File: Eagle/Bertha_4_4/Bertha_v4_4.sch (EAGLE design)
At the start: 115 parts, among them CON1 JACK_DC_BARREL, IC1 MCP1703DB, J1 RJ12RIGHTANGLE-I2C, J2 RJ12RIGHTANGLE-I2C, J7 22--02, Q1 BSP75, Q2 BSP75, Q3 BSP75, Q4 BSP75, Q5 BSP75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

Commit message: Added protection diode on 12V line closes #26
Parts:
- added D1: 1N581D1206, lpatiny:1N581D1206
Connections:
- new net VDD: C1.1, CU3.1, CU7.1, D1.C, D2.C, D4.C, IC1.VI, R12.2, X3-1.1, X3-2.1
- net +12V: now also D1.A; no longer C1.1, CU3.1, CU7.1, D2.C, D4.C, IC1.VI, R12.2, X3-1.1, X3-2.1
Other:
- moved on the sheet: C1, C2, CU3, CU4

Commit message: Added jack connector for PID closes #40
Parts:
- removed J7: 22--02, lpatiny:22--02
- added CON2: JACK_DC_BARREL, lpatiny:JACK_DC_BARREL
- C1, C10, C11, C12, C13, C2, C3, C4, C5, C6, C7, C8, C9, CU1, CU2, CU3, CU4, CU9, CX1, CX2: device rcl:C-EUC1206 -> rcl:C-EUC0805
- RT1, RT2: device resistor:R-EU_R1206 -> resistor:R-EU_R0805
- RUSB1, RUSB2: device resistor:R-EU_M1206 -> resistor:R-EU_M0805
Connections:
- removed net N$36: HX1.D, J7-2.S
- new net N$2: CON2.V+, HX1.D
- net +12V: now also CON2.GND; no longer J7-1.S

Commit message: Changed pin Mapping to allow PWM food control Need to Adapat Arduino code !!!
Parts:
- removed LORA_RST: (no value), Headerlibrary:PINHD-1X1
- CU7, CU8: device rcl:C-EUC1206 -> rcl:C-EUC0805
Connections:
- removed net N$10: R3.1, U$1.CS
- new net MEM_SEL: LDMEM.C, R3.1, U$1.CS
- net A2: now also 100K.2, U100.P$32; no longer R5.1
- net A3: now also R3.2; no longer R6.1
- net D10*: now also R5.1; no longer LDMEM.C, R3.2
- net D5*: now also R6.1; no longer 100K.2, LORA_RST.1, U100.P$32
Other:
- note removed: "LEVEL_Converters"
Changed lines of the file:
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@@
 <part name="GND7" library="supply1" deviceset="GND" device=""/>
 <part name="R1" library="rcl" deviceset="R-EU_" device="R0805" value="1k"/>
-<part name="CU7" library="rcl" deviceset="C-EU" device="C1206" value="10uF"/>
+<part name="CU7" library="rcl" deviceset="C-EU" device="C0805" value="10uF"/>
 <part name="GND19" library="supply1" deviceset="GND" device=""/>
-<part name="CU8" library="rcl" deviceset="C-EU" device="C1206" value="10uF"/>
+<part name="CU8" library="rcl" deviceset="C-EU" device="C0805" value="10uF"/>
 <part name="IC1" library="linear" deviceset="MCP1703" device="DB"/>
 <part name="P+15" library="SparkFun" deviceset="3.3V" device=""/>
@@
 <part name="SJ3" library="jumper" deviceset="SJ" device=""/>
 <part name="U100" library="Octanis1" deviceset="RN2483" device="" value="RN2483"/>
-<part name="LORA_RST" library="Headerlibrary" deviceset="PINHD-1X1" device=""/>
 <part name="GND32" library="supply1" deviceset="GND" device=""/>
 <part name="GND38" library="supply1" deviceset="GND" device=""/>
@@
 <wire x1="48.26" y1="7.62" x2="48.26" y2="68.58" width="1.27" layer="94"/>
 <wire x1="180.34" y1="289.56" x2="299.72" y2="289.56" width="1.27" layer="94"/>
-<text x="106.68" y="60.96" size="5.08" layer="91">LEVEL_Converters</text>
 <wire x1="104.14" y1="68.58" x2="104.14" y2="7.62" width="1.27" layer="94"/>
 <text x="50.8" y="60.96" size="5.08" layer="91">FOOD</text>
@@
 <instance part="SJ3" gate="1" x="142.24" y="149.86" rot="R270"/>
 <instance part="U100" gate="G$1" x="210.82" y="256.54" rot="R270"/>
-<instance part="LORA_RST" gate="G$1" x="251.46" y="281.94"/>
 <instance part="GND32" gate="1" x="246.38" y="157.48" rot="R270"/>
 <instance part="GND38" gate="1" x="228.6" y="142.24"/>
@@
 </segment>
 <segment>
-<label x="114.3" y="20.32" size="1.778" layer="95"/>
-<label x="162.56" y="20.32" size="1.778" layer="95"/>
-<wire x1="114.3" y1="20.32" x2="170.18" y2="20.32" width="0.1524" layer="91"/>
-</segment>
-<segment>
 <pinref part="RK3" gate="G$1" pin="1"/>
 <wire x1="467.36" y1="246.38" x2="472.44" y2="246.38" width="0.1524" layer="91"/>
@@
 </segment>
 <segment>
-<label x="114.3" y="22.86" size="1.778" layer="95"/>
-<label x="162.56" y="22.86" size="1.778" layer="95"/>
-<wire x1="114.3" y1="22.86" x2="170.18" y2="22.86" width="0.1524" layer="91"/>
-</segment>
-<segment>
 <pinref part="U$1" gate="G$1" pin="MISO"/>
 <wire x1="421.64" y1="248.92" x2="396.24" y2="248.92" width="0.1524" layer="91"/>
@@
 </segment>
 <segment>
-<label x="114.3" y="25.4" size="1.778" layer="95"/>
-<label x="162.56" y="25.4" size="1.778" layer="95"/>
-<wire x1="114.3" y1="25.4" x2="170.18" y2="25.4" width="0.1524" layer="91"/>
-</segment>
-<segment>
 <label x="490.22" y="243.84" size="1.778" layer="95"/>
 <label x="459.74" y="243.84" size="1.778" layer="95"/>
@@
 </segment>
 <segment>
-<pinref part="R5" gate="G$1" pin="1"/>
-<wire x1="55.88" y1="50.8" x2="50.8" y2="50.8" width="0.1524" layer="91"/>
-<label x="50.8" y="50.8" size="1.778" layer="95"/>
+<pinref part="100K" gate="G$1" pin="2"/>
+<pinref part="U100" gate="G$1" pin="P$32"/>
+<wire x1="226.06" y1="284.48" x2="226.06" y2="279.4" width="0.1524" layer="91"/>
+<label x="226.06" y="281.94" size="1.778" layer="95"/>
 </segment>
 </net>
@@
 </segment>
 <segment>
-<pinref part="R6" gate="G$1" pin="1"/>
-<wire x1="55.88" y1="25.4" x2="50.8" y2="25.4" width="0.1524" layer="91"/>
-<label x="50.8" y="25.4" size="1.778" layer="95"/>
+<pinref part="R3" gate="G$1" pin="2"/>
+<wire x1="401.32" y1="254" x2="396.24" y2="254" width="0.1524" layer="91"/>
+<label x="396.24" y="254" size="1.778" layer="95"/>
 </segment>
 </net>
@@
 </segment>
 <segment>
-<wire x1="226.06" y1="279.4" x2="226.06" y2="281.94" width="0.1524" layer="91"/>
-<pinref part="U100" gate="G$1" pin="P$32"/>
-<label x="246.38" y="276.86" size="1.778" layer="95"/>
-<pinref part="LORA_RST" gate="G$1" pin="1"/>
-<wire x1="226.06" y1="281.94" x2="226.06" y2="284.48" width="0.1524" layer="91"/>
-<wire x1="248.92" y1="281.94" x2="226.06" y2="281.94" width="0.1524" layer="91"/>
-<junction x="226.06" y="281.94"/>
-<pinref part="100K" gate="G$1" pin="2"/>
-<label x="243.84" y="274.32" size="1.778" layer="95"/>
+<pinref part="R6" gate="G$1" pin="1"/>
+<wire x1="55.88" y1="25.4" x2="50.8" y2="25.4" width="0.1524" layer="91"/>
+<label x="55.88" y="27.94" size="1.778" layer="95" rot="R180"/>
 </segment>
 </net>
@@
 </segment>
 <segment>
-<label x="162.56" y="43.18" size="1.778" layer="95"/>
-<label x="116.84" y="43.18" size="1.778" layer="95"/>
-<wire x1="170.18" y1="43.18" x2="116.84" y2="43.18" width="0.1524" layer="91"/>
-</segment>
-<segment>
-<pinref part="LDMEM" gate="G$1" pin="C"/>
-<wire x1="436.88" y1="22.86" x2="436.88" y2="12.7" width="0.1524" layer="91"/>
-<label x="436.88" y="12.7" size="1.778" layer="95" rot="R90"/>
-</segment>
-<segment>
-<pinref part="R3" gate="G$1" pin="2"/>
-<wire x1="401.32" y1="254" x2="396.24" y2="254" width="0.1524" layer="91"/>
-<label x="391.16" y="254" size="1.778" layer="95"/>
-<wire x1="398.78" y1="254" x2="401.32" y2="254" width="0.1524" layer="91"/>
-<junction x="401.32" y="254"/>
+<pinref part="R5" gate="G$1" pin="1"/>
+<wire x1="55.88" y1="50.8" x2="50.8" y2="50.8" width="0.1524" layer="91"/>
+<label x="50.8" y="50.8" size="1.778" layer="95"/>
 </segment>
 </net>
@@
 </segment>
 </net>
-<net name="N$10" class="0">
-<segment>
-<wire x1="421.64" y1="251.46" x2="414.02" y2="251.46" width="0.1524" layer="91"/>
-<wire x1="414.02" y1="251.46" x2="414.02" y2="254" width="0.1524" layer="91"/>
-<wire x1="414.02" y1="254" x2="411.48" y2="254" width="0.1524" layer="91"/>
-<pinref part="R3" gate="G$1" pin="1"/>
-<pinref part="U$1" gate="G$1" pin="CS"/>
-</segment>
-</net>
 <net name="SDA" class="0">
 <segment>
@@
 </segment>
 <segment>
-<label x="162.56" y="48.26" size="1.778" layer="95"/>
-<label x="116.84" y="48.26" size="1.778" layer="95"/>
-<wire x1="170.18" y1="48.26" x2="116.84" y2="48.26" width="0.1524" layer="91"/>
-</segment>
-<segment>
 <pinref part="U100" gate="G$1" pin="P$7"/>
 <wire x1="203.2" y1="233.68" x2="203.2" y2="228.6" width="0.1524" layer="91"/>
@@
 </segment>
 <segment>
-<label x="116.84" y="50.8" size="1.778" layer="95"/>
-<label x="162.56" y="50.8" size="1.778" layer="95"/>
-<wire x1="116.84" y1="50.8" x2="170.18" y2="50.8" width="0.1524" layer="91"/>
-</segment>
-<segment>
 <pinref part="U100" gate="G$1" pin="P$6"/>
 <wire x1="200.66" y1="233.68" x2="200.66" y2="228.6" width="0.1524" layer="91"/>
@@
 </segment>
 <segment>
-<pinref part="U100" gate="G$1" pin="P$28"/>
 <pinref part="U100" gate="G$1" pin="P$33"/>
-<wire x1="236.22" y1="279.4" x2="223.52" y2="279.4" width="0.1524" layer="91"/>
 <wire x1="223.52" y1="279.4" x2="223.52" y2="284.48" width="0.1524" layer="91"/>
-<junction x="223.52" y="279.4"/>
 <pinref part="U100" gate="G$1" pin="P$41"/>
 <wire x1="223.52" y1="284.48" x2="203.2" y2="284.48" width="0.1524" layer="91"/>
@@
 <junction x="203.2" y="284.48"/>
 <label x="193.04" y="284.48" size="1.778" layer="95"/>
+<pinref part="U100" gate="G$1" pin="P$28"/>
+<wire x1="223.52" y1="279.4" x2="236.22" y2="279.4" width="0.1524" layer="91"/>
+<junction x="223.52" y="279.4"/>
 </segment>
 <segment>
@@
 </segment>
 </net>
+<net name="MEM_SEL" class="0">
+<segment>
+<pinref part="LDMEM" gate="G$1" pin="C"/>
+<wire x1="436.88" y1="22.86" x2="436.88" y2="12.7" width="0.1524" layer="91"/>
+<label x="436.88" y="12.7" size="1.778" layer="95" rot="R90"/>
+</segment>
+<segment>
+<wire x1="421.64" y1="251.46" x2="414.02" y2="251.46" width="0.1524" layer="91"/>
+<wire x1="414.02" y1="251.46" x2="414.02" y2="254" width="0.1524" layer="91"/>
+<wire x1="414.02" y1="254" x2="411.48" y2="254" width="0.1524" layer="91"/>
+<pinref part="R3" gate="G$1" pin="1"/>
+<pinref part="U$1" gate="G$1" pin="CS"/>
+<label x="414.02" y="254" size="1.778" layer="95" rot="R90"/>
+</segment>
+</net>

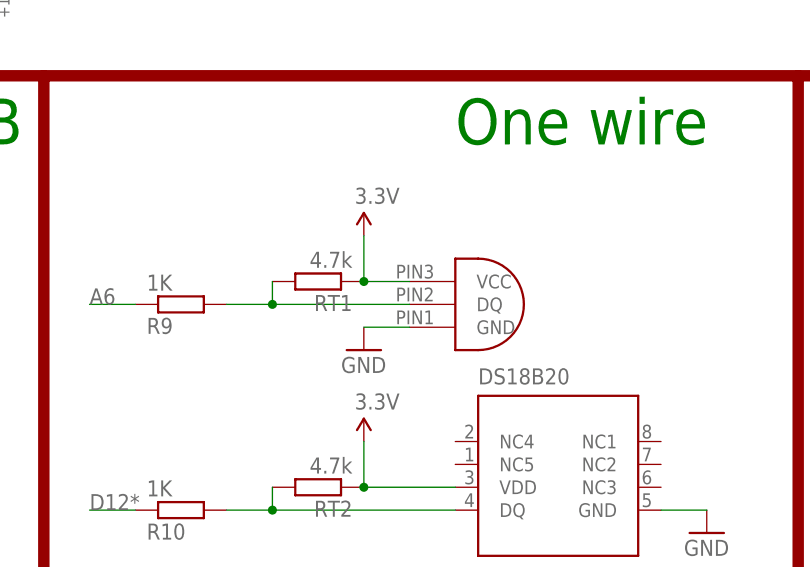
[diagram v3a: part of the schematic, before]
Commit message: Added Jack connector for DS18B20 closes #24
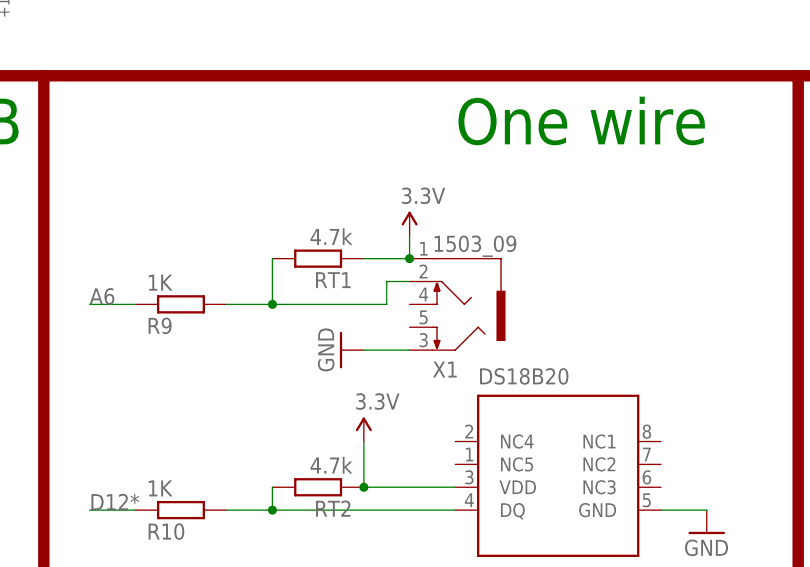
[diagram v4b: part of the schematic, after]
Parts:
- removed U$8: DS18B20_SMALLPADS, lpatiny:DS18B20_SMALLPADS
- added X1: 1503_09, con-lumberg:1503_09
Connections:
- net 3.3V: now also X1.1; no longer U$8.VCC
- net GND: now also X1.3; no longer U$8.GND
- net N$21: now also X1.2; no longer U$8.DQ
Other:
- moved on the sheet: RT1
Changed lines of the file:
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@@
 <grid distance="0.1" unitdist="inch" unit="inch" style="lines" multiple="1" display="no" altdistance="0.01" altunitdist="inch" altunit="inch"/>
 <layers>
-<layer number="1" name="Top" color="4" fill="1" visible="yes" active="no"/>
-<layer number="16" name="Bottom" color="1" fill="1" visible="yes" active="no"/>
-<layer number="17" name="Pads" color="2" fill="1" visible="yes" active="no"/>
-<layer number="18" name="Vias" color="2" fill="1" visible="yes" active="no"/>
-<layer number="19" name="Unrouted" color="6" fill="1" visible="yes" active="no"/>
-<layer number="20" name="Dimension" color="15" fill="1" visible="yes" active="no"/>
-<layer number="21" name="tPlace" color="7" fill="1" visible="yes" active="no"/>
-<layer number="22" name="bPlace" color="7" fill="1" visible="yes" active="no"/>
-<layer number="23" name="tOrigins" color="15" fill="1" visible="yes" active="no"/>
-<layer number="24" name="bOrigins" color="15" fill="1" visible="yes" active="no"/>
-<layer number="25" name="tNames" color="7" fill="1" visible="yes" active="no"/>
-<layer number="26" name="bNames" color="7" fill="1" visible="yes" active="no"/>
-<layer number="27" name="tValues" color="7" fill="1" visible="yes" active="no"/>
-<layer number="28" name="bValues" color="7" fill="1" visible="yes" active="no"/>
+<layer number="1" name="Top" color="4" fill="1" visible="no" active="no"/>
+<layer number="16" name="Bottom" color="1" fill="1" visible="no" active="no"/>
+<layer number="17" name="Pads" color="2" fill="1" visible="no" active="no"/>
+<layer number="18" name="Vias" color="2" fill="1" visible="no" active="no"/>
+<layer number="19" name="Unrouted" color="6" fill="1" visible="no" active="no"/>
+<layer number="20" name="Dimension" color="15" fill="1" visible="no" active="no"/>
+<layer number="21" name="tPlace" color="7" fill="1" visible="no" active="no"/>
+<layer number="22" name="bPlace" color="7" fill="1" visible="no" active="no"/>
+<layer number="23" name="tOrigins" color="15" fill="1" visible="no" active="no"/>
+<layer number="24" name="bOrigins" color="15" fill="1" visible="no" active="no"/>
+<layer number="25" name="tNames" color="7" fill="1" visible="no" active="no"/>
+<layer number="26" name="bNames" color="7" fill="1" visible="no" active="no"/>
+<layer number="27" name="tValues" color="7" fill="1" visible="no" active="no"/>
+<layer number="28" name="bValues" color="7" fill="1" visible="no" active="no"/>
 <layer number="29" name="tStop" color="7" fill="3" visible="no" active="no"/>
 <layer number="30" name="bStop" color="7" fill="6" visible="no" active="no"/>
@@
 <layer number="35" name="tGlue" color="7" fill="4" visible="no" active="no"/>
 <layer number="36" name="bGlue" color="7" fill="5" visible="no" active="no"/>
-<layer number="37" name="tTest" color="7" fill="1" visible="yes" active="no"/>
-<layer number="38" name="bTest" color="7" fill="1" visible="yes" active="no"/>
+<layer number="37" name="tTest" color="7" fill="1" visible="no" active="no"/>
+<layer number="38" name="bTest" color="7" fill="1" visible="no" active="no"/>
 <layer number="39" name="tKeepout" color="4" fill="11" visible="no" active="no"/>
 <layer number="40" name="bKeepout" color="1" fill="11" visible="no" active="no"/>
@@
 <layer number="44" name="Drills" color="7" fill="1" visible="no" active="no"/>
 <layer number="45" name="Holes" color="7" fill="1" visible="no" active="no"/>
-<layer number="46" name="Milling" color="3" fill="1" visible="yes" active="no"/>
-<layer number="47" name="Measures" color="7" fill="1" visible="yes" active="no"/>
-<layer number="48" name="Document" color="7" fill="1" visible="yes" active="no"/>
-<layer number="49" name="Reference" color="7" fill="1" visible="yes" active="no"/>
-<layer number="50" name="dxf" color="12" fill="1" visible="yes" active="no"/>
-<layer number="51" name="tDocu" color="7" fill="1" visible="yes" active="no"/>
-<layer number="52" name="bDocu" color="7" fill="1" visible="yes" active="no"/>
-<layer number="53" name="tGND_GNDA" color="7" fill="1" visible="yes" active="no"/>
-<layer number="54" name="bGND_GNDA" color="7" fill="1" visible="yes" active="no"/>
-<layer number="56" name="wert" color="7" fill="1" visible="yes" active="no"/>
-<layer number="57" name="tCAD" color="7" fill="1" visible="yes" active="no"/>
-<layer number="59" name="tCarbon" color="7" fill="1" visible="yes" active="no"/>
-<layer number="60" name="bCarbon" color="7" fill="1" visible="yes" active="no"/>
+<layer number="46" name="Milling" color="3" fill="1" visible="no" active="no"/>
+<layer number="47" name="Measures" color="7" fill="1" visible="no" active="no"/>
+<layer number="48" name="Document" color="7" fill="1" visible="no" active="no"/>
+<layer number="49" name="Reference" color="7" fill="1" visible="no" active="no"/>
+<layer number="50" name="dxf" color="12" fill="1" visible="no" active="no"/>
+<layer number="51" name="tDocu" color="7" fill="1" visible="no" active="no"/>
+<layer number="52" name="bDocu" color="7" fill="1" visible="no" active="no"/>
+<layer number="53" name="tGND_GNDA" color="7" fill="1" visible="no" active="no"/>
+<layer number="54" name="bGND_GNDA" color="7" fill="1" visible="no" active="no"/>
+<layer number="56" name="wert" color="7" fill="1" visible="no" active="no"/>
+<layer number="57" name="tCAD" color="7" fill="1" visible="no" active="no"/>
+<layer number="59" name="tCarbon" color="7" fill="1" visible="no" active="no"/>
+<layer number="60" name="bCarbon" color="7" fill="1" visible="no" active="no"/>
 <layer number="90" name="Modules" color="5" fill="1" visible="no" active="no"/>
 <layer number="91" name="Nets" color="2" fill="1" visible="yes" active="yes"/>
@@
 <part name="J1" library="lpatiny" deviceset="RJ12" device="RIGHTANGLE-I2C"/>
 <part name="J2" library="lpatiny" deviceset="RJ12" device="RIGHTANGLE-I2C"/>
-<part name="U$8" library="lpatiny" deviceset="DS18B20_SMALLPADS" device=""/>
 <part name="P+23" library="supply1" deviceset="+12V" device=""/>
 <part name="P+24" library="supply1" deviceset="+12V" device=""/>
@@
 <part name="SUPPLY5" library="supply2" deviceset="VDD" device=""/>
 <part name="CON2" library="lpatiny" deviceset="JACK_DC_BARREL" device=""/>
+<part name="X1" library="con-lumberg" deviceset="1503_09" device=""/>
 </parts>
 <sheets>
@@
 </instance>
 <instance part="GND2" gate="1" x="360.68" y="10.16"/>
-<instance part="GND11" gate="1" x="274.32" y="38.1"/>
-<instance part="RT1" gate="G$1" x="269.24" y="45.72" rot="R180"/>
+<instance part="GND11" gate="1" x="271.78" y="38.1" rot="R270"/>
+<instance part="RT1" gate="G$1" x="269.24" y="48.26" rot="R180"/>
 <instance part="GND20" gate="1" x="312.42" y="17.78"/>
 <instance part="RT2" gate="G$1" x="269.24" y="22.86" rot="R180"/>
@@
 <instance part="J1" gate="G$1" x="368.3" y="271.78"/>
 <instance part="J2" gate="G$1" x="368.3" y="241.3"/>
-<instance part="U$8" gate="G$1" x="284.48" y="43.18" rot="R270"/>
 <instance part="P+23" gate="1" x="482.6" y="121.92" rot="R90"/>
 <instance part="P+24" gate="1" x="482.6" y="114.3" rot="R90"/>
@@
 <instance part="P+35" gate="G$1" x="30.48" y="116.84"/>
 <instance part="P+36" gate="G$1" x="274.32" y="27.94"/>
-<instance part="P+37" gate="G$1" x="274.32" y="50.8"/>
+<instance part="P+37" gate="G$1" x="279.4" y="50.8"/>
 <instance part="P+39" gate="G$1" x="401.32" y="45.72"/>
 <instance part="P+40" gate="G$1" x="408.94" y="45.72"/>
@@
 <instance part="SUPPLY5" gate="G$1" x="464.82" y="45.72"/>
 <instance part="CON2" gate="G$1" x="367.538" y="44.45" rot="R90"/>
+<instance part="X1" gate="G$1" x="284.48" y="43.18" rot="MR180"/>
 </instances>
 <busses>
@@
 </segment>
 <segment>
-<pinref part="GND11" gate="1" pin="GND"/>
-<wire x1="274.32" y1="40.64" x2="279.4" y2="40.64" width="0.1524" layer="91"/>
-<pinref part="U$8" gate="G$1" pin="GND"/>
-</segment>
-<segment>
 <wire x1="419.1" y1="22.86" x2="419.1" y2="15.24" width="0.1524" layer="91"/>
 <pinref part="GND21" gate="1" pin="GND"/>
@@
 <wire x1="231.14" y1="111.76" x2="220.98" y2="111.76" width="0.1524" layer="91"/>
 </segment>
+<segment>
+<pinref part="X1" gate="G$1" pin="3"/>
+<pinref part="GND11" gate="1" pin="GND"/>
+<wire x1="274.32" y1="38.1" x2="279.4" y2="38.1" width="0.1524" layer="91"/>
+</segment>
 </net>
 <net name="SCK" class="0">
@@
 <segment>
 <pinref part="RT1" gate="G$1" pin="1"/>
-<wire x1="274.32" y1="45.72" x2="279.4" y2="45.72" width="0.1524" layer="91"/>
-<wire x1="274.32" y1="50.8" x2="274.32" y2="45.72" width="0.1524" layer="91"/>
-<junction x="274.32" y="45.72"/>
-<pinref part="U$8" gate="G$1" pin="VCC"/>
 <pinref part="P+37" gate="G$1" pin="3.3V"/>
+<wire x1="279.4" y1="50.8" x2="279.4" y2="48.26" width="0.1524" layer="91"/>
+<pinref part="X1" gate="G$1" pin="1"/>
+<junction x="279.4" y="48.26"/>
+<wire x1="279.4" y1="48.26" x2="274.32" y2="48.26" width="0.1524" layer="91"/>
 </segment>
 <segment>
@@
 <net name="N$21" class="1">
 <segment>
-<wire x1="279.4" y1="43.18" x2="264.16" y2="43.18" width="0.1524" layer="91"/>
 <pinref part="RT1" gate="G$1" pin="2"/>
-<wire x1="264.16" y1="45.72" x2="264.16" y2="43.18" width="0.1524" layer="91"/>
+<wire x1="276.86" y1="43.18" x2="264.16" y2="43.18" width="0.1524" layer="91"/>
+<wire x1="264.16" y1="48.26" x2="264.16" y2="43.18" width="0.1524" layer="91"/>
 <wire x1="264.16" y1="43.18" x2="259.08" y2="43.18" width="0.1524" layer="91"/>
 <pinref part="R9" gate="G$1" pin="2"/>
 <junction x="264.16" y="43.18"/>
-<pinref part="U$8" gate="G$1" pin="DQ"/>
+<pinref part="X1" gate="G$1" pin="2"/>
+<wire x1="279.4" y1="45.72" x2="276.86" y2="45.72" width="0.1524" layer="91"/>
+<wire x1="276.86" y1="45.72" x2="276.86" y2="43.18" width="0.1524" layer="91"/>
 </segment>
 </net>
